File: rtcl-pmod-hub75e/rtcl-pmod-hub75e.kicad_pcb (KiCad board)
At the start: 4 copper layers, 20 x 56 mm, 24 parts, among them J1 PMOD, J2 HIF3FC-16PA-2.54DSA(71), J3 Conn_01x02, U1 74LVC273, U2 74LVC273, U3 74LVC273, U4 74LVC273, U5 LM809M3-2.93, U6 74LVC2G86

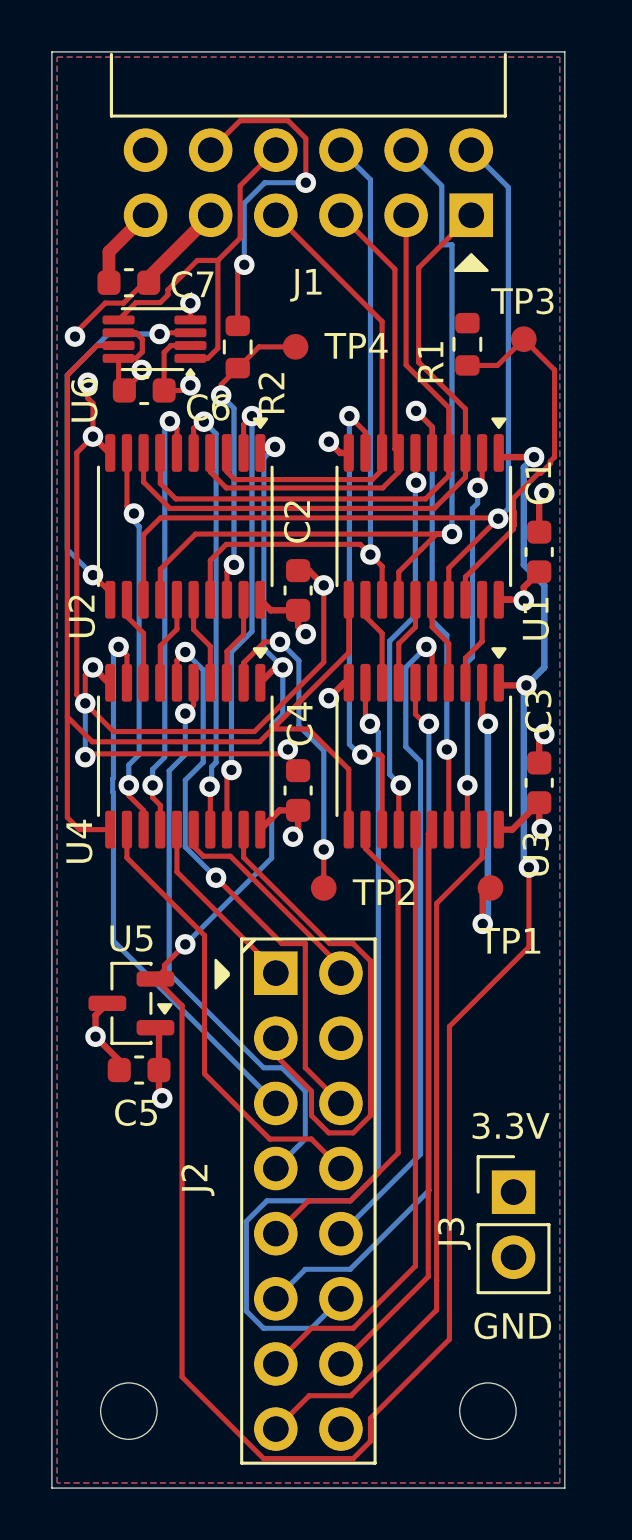
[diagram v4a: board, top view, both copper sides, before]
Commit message: Update KiCad project files and component model for PH_02x06_2.54mm
- Changed active layer in rtcl-pmod-hub75e.kicad_prl from 4 to 0.
- Updated UUIDs for various properties and elements in PH_02x06_2.54mm.kicad_mod.
- Added embedded model for PH_02x06_2.54mm component with specified offset, scale, and rotation.
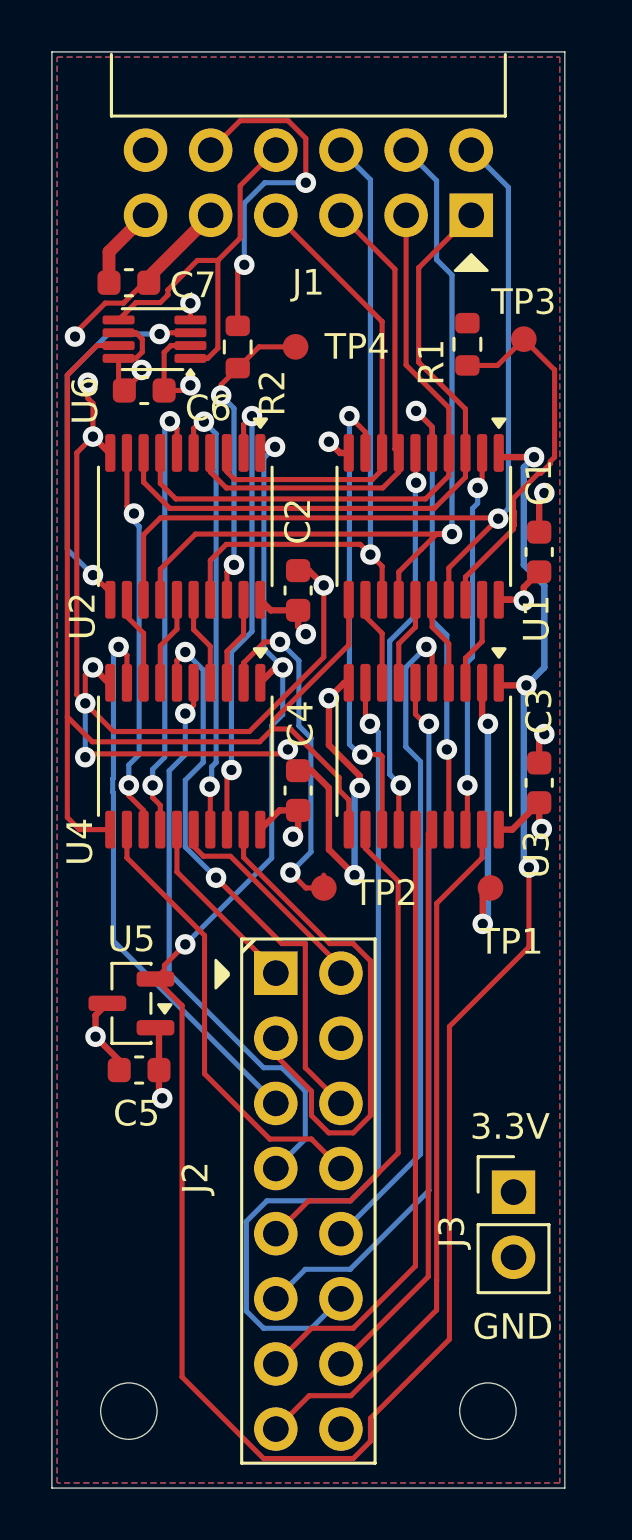
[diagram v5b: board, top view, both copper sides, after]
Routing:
- net GND: track 76.9 -> 89.6 mm, vias 17 -> 19
- net Net-(U4-Q0): track 13.2 -> 14.3 mm
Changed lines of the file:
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@@
 		(tags "Through hole pin header THT 2x06 2.54mm double row")
 		(property "Reference" "J1"
-			(at 3.9 0 180)
+			(at 3.9 0 0)
 			(layer "F.SilkS")
 			(effects
@@
 		(sheetname "/")
 		(sheetfile "rtcl-pmod-hub75e.kicad_sch")
-		(units
-			(unit
-				(name "A")
-				(pins "1" "2" "3" "4" "5" "6" "7" "8" "9" "10" "11" "12")
-			)
-		)
 		(attr through_hole)
 		(duplicate_pad_numbers_are_jumpers no)
@@
 		)
 		(embedded_fonts no)
+		(model "C:/Users/ryuji/OneDrive/Documents/Development/kicad/rtcl-pmod-hub75e/model/PH2RA-12-UA.STEP"
+			(offset
+				(xyz -4 -6 2.5)
+			)
+			(scale
+				(xyz 1 1 1)
+			)
+			(rotate
+				(xyz -0 180 -90)
+			)
+		)
 	)
 	(footprint "MountingHole:MountingHole_2.2mm_M2"
@@
 	)
 	(segment
-		(start 107.9 76.5)
-		(end 110.6 73.8)
-		(width 0.2)
-		(layer "F.Cu")
-		(net "GND")
-	)
-	(segment
 		(start 102.793776 59.793776)
 		(end 103.587552 59)
@@
 	)
 	(segment
+		(start 110.6 73.6)
+		(end 110.6 70.8)
+		(width 0.2)
+		(layer "F.Cu")
+		(net "GND")
+	)
+	(segment
 		(start 109.6 70.225)
 		(end 110.025 70.225)
@@
 	)
 	(segment
-		(start 102.4 76.5)
-		(end 107.9 76.5)
-		(width 0.2)
+		(start 110.8 78.7)
+		(end 110.8 81.1)
+		(width 0.25)
 		(layer "F.Cu")
 		(net "GND")
@@
 	)
 	(segment
+		(start 102.4 76.5)
+		(end 107.7 76.5)
+		(width 0.2)
+		(layer "F.Cu")
+		(net "GND")
+	)
+	(segment
+		(start 110.8 81.1)
+		(end 111.8 82.1)
+		(width 0.25)
+		(layer "F.Cu")
+		(net "GND")
+	)
+	(segment
 		(start 104.175 90.675)
 		(end 104.3 90.8)
@@
 	)
 	(segment
-		(start 101.3 75.4)
-		(end 102.4 76.5)
-		(width 0.2)
+		(start 112 78.7)
+		(end 112 78.22631)
+		(width 0.25)
+		(layer "F.Cu")
+		(net "GND")
+	)
+	(segment
+		(start 110.8 77.02631)
+		(end 110.8 75.2)
+		(width 0.25)
 		(layer "F.Cu")
 		(net "GND")
@@
 	)
 	(segment
+		(start 101.3 75.4)
+		(end 102.4 76.5)
+		(width 0.2)
+		(layer "F.Cu")
+		(net "GND")
+	)
+	(segment
+		(start 110.125 78.025)
+		(end 110.8 78.7)
+		(width 0.25)
+		(layer "F.Cu")
+		(net "GND")
+	)
+	(segment
 		(start 119 68.725)
 		(end 119 67.4)
@@
 	)
 	(segment
+		(start 107.7 76.5)
+		(end 110.6 73.6)
+		(width 0.2)
+		(layer "F.Cu")
+		(net "GND")
+	)
+	(segment
 		(start 101.43 77.37)
 		(end 101.3 77.5)
@@
 	)
 	(segment
+		(start 112 78.22631)
+		(end 110.8 77.02631)
+		(width 0.25)
+		(layer "F.Cu")
+		(net "GND")
+	)
+	(segment
 		(start 110.025 70.225)
 		(end 110.6 70.8)
@@
 	)
 	(segment
-		(start 110.6 73.8)
-		(end 110.6 70.8)
-		(width 0.2)
-		(layer "F.Cu")
-		(net "GND")
-	)
-	(segment
 		(start 103.775 59)
 		(end 103.775 58.785)
@@
 		(net "GND")
 	)
+	(segment
+		(start 109.6 78.025)
+		(end 110.125 78.025)
+		(width 0.25)
+		(layer "F.Cu")
+		(net "GND")
+	)
 	(via
 		(at 105.4 63)
@@
 	)
 	(via
+		(at 111.8 82.1)
+		(size 0.8)
+		(drill 0.4)
+		(layers "F.Cu" "B.Cu")
+		(net "GND")
+	)
+	(via
 		(at 107.5 58.3)
 		(size 0.8)
@@
 	)
 	(via
+		(at 112 78.7)
+		(size 0.8)
+		(drill 0.4)
+		(layers "F.Cu" "B.Cu")
+		(net "GND")
+	)
+	(via
 		(at 100.9 61.1)
 		(size 0.8)
@@
 	)
 	(segment
+		(start 111.8 78.9)
+		(end 112 78.7)
+		(width 0.25)
+		(layer "B.Cu")
+		(net "GND")
+	)
+	(segment
 		(start 108.3 55.1)
 		(end 109.9 55.1)
@@
 	)
 	(segment
+		(start 111.8 82.1)
+		(end 111.8 78.9)
+		(width 0.25)
+		(layer "B.Cu")
+		(net "GND")
+	)
+	(segment
 		(start 101.4 62.9)
 		(end 100.9 62.4)
@@
 	)
 	(segment
+		(start 111.575 80.8625)
+		(end 111.575 79.165955)
+		(width 0.2)
+		(layer "F.Cu")
+		(net "/CLK_P")
+	)
+	(segment
+		(start 108.6 76.1)
+		(end 108.6 76.4)
+		(width 0.2)
+		(layer "F.Cu")
+		(net "/CLK_P")
+	)
+	(segment
 		(start 102.6 61.45)
 		(end 101.75 61.45)
@@
 	)
 	(segment
-		(start 110 76.4)
-		(end 108.6 76.4)
+		(start 101.75 61.45)
+		(end 100.6 62.6)
 		(width 0.2)
 		(layer "F.Cu")
@@
 	)
 	(segment
-		(start 101.75 61.45)
-		(end 100.6 62.6)
+		(start 111.575 73.125)
+		(end 108.6 76.1)
 		(width 0.2)
 		(layer "F.Cu")
@@
 	)
 	(segment
-		(start 111.575 71.3625)
-		(end 111.575 73.425)
+		(start 111.2 78.790955)
+		(end 111.2 78.3)
 		(width 0.2)
 		(layer "F.Cu")
@@
 	)
 	(segment
-		(start 111.575 73.425)
-		(end 108.6 76.4)
+		(start 100.6 75.925)
+		(end 100.6 79.85)
 		(width 0.2)
 		(layer "F.Cu")
@@
 	)
 	(segment
-		(start 100.6 75.925)
-		(end 100.6 79.85)
+		(start 111.575 79.165955)
+		(end 111.2 78.790955)
+		(width 0.2)
+		(layer "F.Cu")
+		(net "/CLK_P")
+	)
+	(segment
+		(start 109.3 76.4)
+		(end 108.6 76.4)
 		(width 0.2)
 		(layer "F.Cu")
@@
 	)
 	(segment
-		(start 111.575 80.8625)
-		(end 111.575 77.975)
+		(start 111.2 78.3)
+		(end 109.3 76.4)
 		(width 0.2)
 		(layer "F.Cu")
@@
 	)
 	(segment
-		(start 111.575 77.975)
-		(end 110 76.4)
+		(start 111.575 71.3625)
+		(end 111.575 73.125)
 		(width 0.2)
 		(layer "F.Cu")
@@
 	)
 	(segment
+		(start 110.6 82.6)
+		(end 109.9 82.6)
+		(width 0.2)
+		(layer "F.Cu")
+		(net "Net-(U4-Q0)")
+	)
+	(segment
 		(start 107.475 73.825)
 		(end 107.475 74.6)
@@
 	)
 	(segment
-		(start 110.6 82.6)
-		(end 110.6 81.1)
+		(start 110.6 82.5)
+		(end 110.6 82.1)
 		(width 0.2)
 		(layer "F.Cu")
@@
 	)
 	(segment
-		(start 110.6 82.5)
-		(end 110.6 82.1)
+		(start 109.9 82.6)
+		(end 109.3 82)
 		(width 0.2)
 		(layer "F.Cu")
@@
 	)
 	(via
-		(at 110.6 81.1)
+		(at 109.3 82)
 		(size 0.8)
 		(drill 0.4)
@@
 	(segment
 		(start 109.63 76.278448)
-		(end 110.6 77.248448)
+		(end 109.63 73.739045)
 		(width 0.2)
 		(layer "B.Cu")
@@
 	)
 	(segment
-		(start 109.63 73.739045)
+		(start 110.1 76.748448)
 		(end 109.63 76.278448)
 		(width 0.2)
@@
 	)
 	(segment
-		(start 110.6 77.248448)
-		(end 110.6 81.1)
+		(start 109.3 82)
+		(end 110.1 81.2)
 		(width 0.2)
 		(layer "B.Cu")
@@
 	)
 	(segment
-		(start 108.895477 73.004523)
-		(end 109.63 73.739045)
+		(start 110.1 81.2)
+		(end 110.1 76.748448)
+		(width 0.2)
+		(layer "B.Cu")
+		(net "Net-(U4-Q0)")
+	)
+	(segment
+		(start 109.63 73.739045)
+		(end 108.895477 73.004523)
 		(width 0.2)
 		(layer "B.Cu")
@@
 	)
 	(segment
-		(start 115.6 57.52)
-		(end 115.2 57.52)
+		(start 115 55.02)
+		(end 113.81 53.83)
 		(width 0.2)
 		(layer "B.Cu")
@@
 	)
 	(segment
-		(start 115.2 57.52)
-		(end 115.2 55.22)
+		(start 115.6 68.8)
+		(end 115.6 58.7)
 		(width 0.2)
 		(layer "B.Cu")
@@
 	)
 	(segment
-		(start 115.2 55.22)
-		(end 113.81 53.83)
+		(start 115 58.1)
+		(end 115 55.02)
 		(width 0.2)
 		(layer "B.Cu")
@@
 	)
 	(segment
-		(start 115.6 68.8)
-		(end 115.6 57.52)
+		(start 115.6 58.7)
+		(end 115 58.1)
 		(width 0.2)
 		(layer "B.Cu")
